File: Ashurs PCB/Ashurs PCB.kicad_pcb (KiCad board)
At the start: 4 copper layers, 75 x 25 mm, 58 parts, among them J1 3220-20-0200-00, J2 GSB1C41110SSHR, J3 1984617, J4 647676-2, Q1 NMOS, U1 BNO055, U2 LMS8117AMP-3.3, U3 SST25VF010A-33-4C-SAE, U4 BMP390, U5 CP2102N-A02-GQFN20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

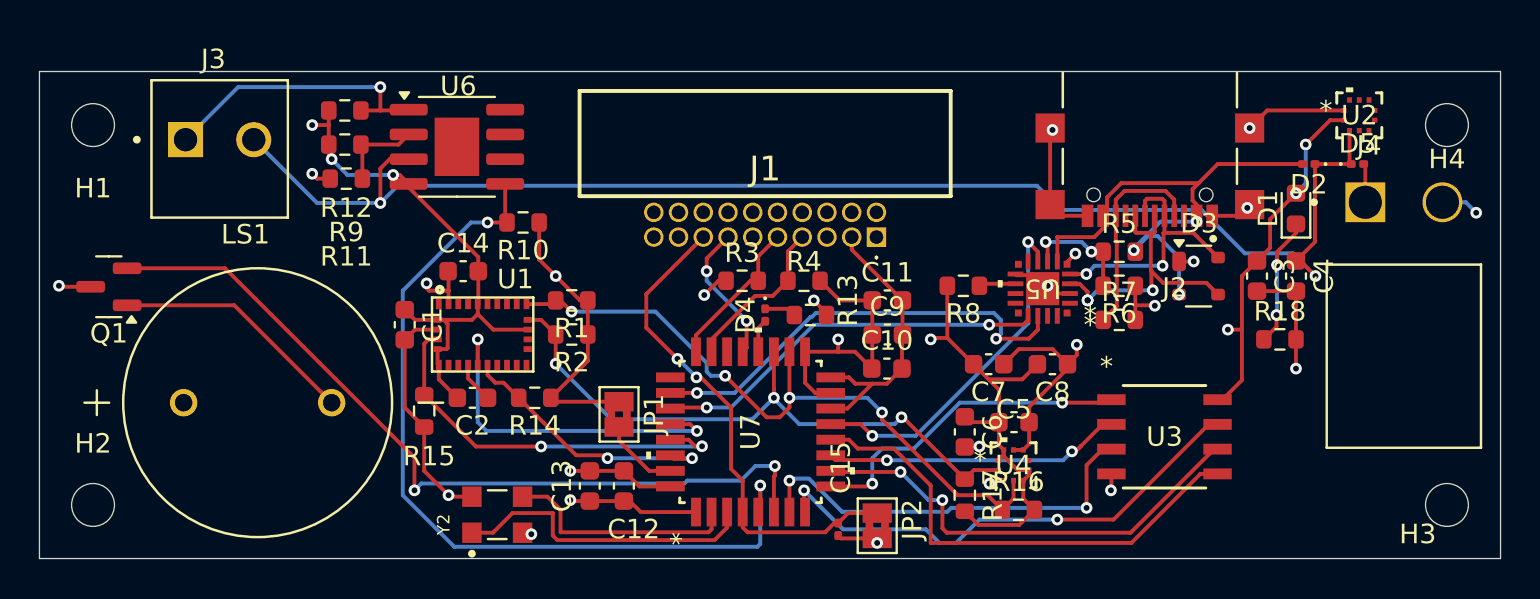
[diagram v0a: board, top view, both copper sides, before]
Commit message: post-david suggestions
u6 footprint, zener diode footprints, jumper footprints
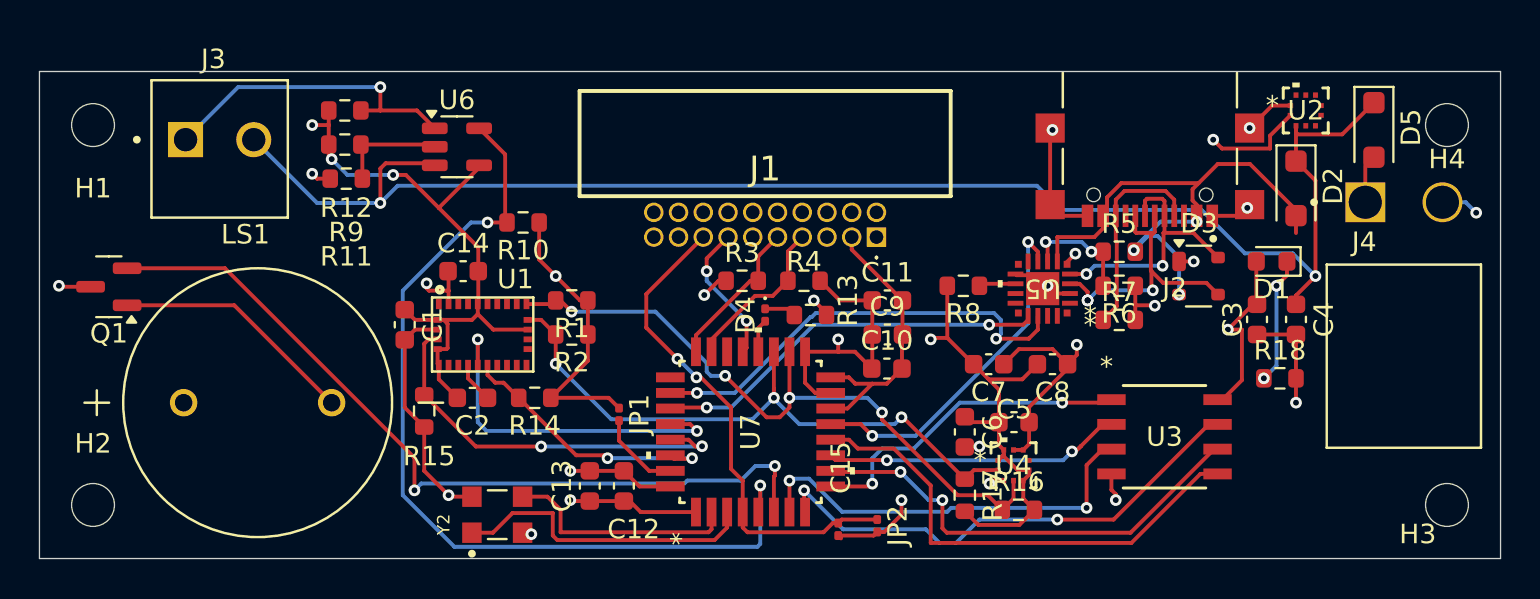
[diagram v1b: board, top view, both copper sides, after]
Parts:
- D2, D5: footprint Diode_SMD:D_0201_0603Metric -> Diode_SMD:D_SOD-123F
- JP1, JP2: footprint Jumper:SolderJumper-2_P1.3mm_Bridged2Bar_Pad1.0x1.5mm -> Resistor_SMD:R_0201_0603Metric
- U6: footprint Package_SO:SOIC-8-1EP_3.9x4.9mm_P1.27mm_EP2.29x3mm -> Package_TO_SOT_SMD:SOT-23-5
- moved D1 2.99 mm to (208.8, 47.8), turned to 180 degrees
- moved U2 2.76 mm to (210.5, 40.0)
- moved C3 2.23 mm to (208.0, 50.7)
- moved C4 2.23 mm to (210.0, 50.7)
- moved R18 2.00 mm to (209.2, 53.8)
- moved D5 1.94 mm to (214.0, 41.0), turned to -90 degrees
- moved D2 1.41 mm to (210.0, 44.0), turned to -90 degrees
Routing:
- net VIN: track 71.5 -> 77.9 mm
- net GND: track 91.1 -> 94.5 mm
- net SWITCH: track 43.0 -> 46.4 mm
- net +3V3: track 94.9 -> 91.9 mm, vias 12 -> 11
- net Net-(U6-+): track 14.7 -> 16.5 mm
- net VBUS: track 26.7 -> 28.1 mm
- net Net-(U6--): track 4.35 -> 5.52 mm

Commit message: Gerber and CSV's
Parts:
- Q1: footprint Package_TO_SOT_SMD:SOT-23 -> Package_TO_SOT_SMD:TSOT-23
- moved Q1 0.86 mm to (148.8, 48.2)
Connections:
- U5 pad 17: USB_RXD -> USB_TXD
- U5 pad 18: USB_TXD -> USB_RXD
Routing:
- net USB_TXD: track 22.9 -> 20.6 mm
- net USB_RXD: track 20.2 -> 21.4 mm
- net GND: track 94.5 -> 95.4 mm

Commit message: footprint mistake
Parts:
- U2: footprint footprint:10LGA_2X2X0p75_BOS -> footprint:MP04A_TEX
- moved U2 19.4 mm to (208.0, 59.2)
- moved U3 2.93 mm to (200.5, 55.8), turned to 90 degrees
- moved C8 1.75 mm to (195.8, 53.0)
- moved C7 1.73 mm to (192.5, 53.0)
- moved D5 0.25 mm to (214.0, 40.8)
- moved J4 0.25 mm to (213.6, 44.5)
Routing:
- net VIN: track 77.9 -> 90.9 mm
- net +3V3: track 91.9 -> 95.6 mm, vias 11 -> 12
- net Flash_SO: track 15.0 -> 17.9 mm
- net Flash_SI: track 25.3 -> 27.4 mm
- net GND: track 95.4 -> 96.6 mm, vias 20 -> 21
- net Flash_WP: track 21.1 -> 21.9 mm
- net Flash_SCK: track 23.5 -> 24.2 mm, vias 2 -> 4
- net LIPO_POWER: track 1.88 -> 2.50 mm
